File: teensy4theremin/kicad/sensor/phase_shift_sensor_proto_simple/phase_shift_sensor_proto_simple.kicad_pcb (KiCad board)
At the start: 2 copper layers, 94 x 35.6 mm, 23 parts, among them J1 INDUCTOR_IN, J2 INDUCTOR_OUT, J3 ANTENNA, J4 SENSOR, U1 74HC04, U2 sp721, U3 REG_3V3

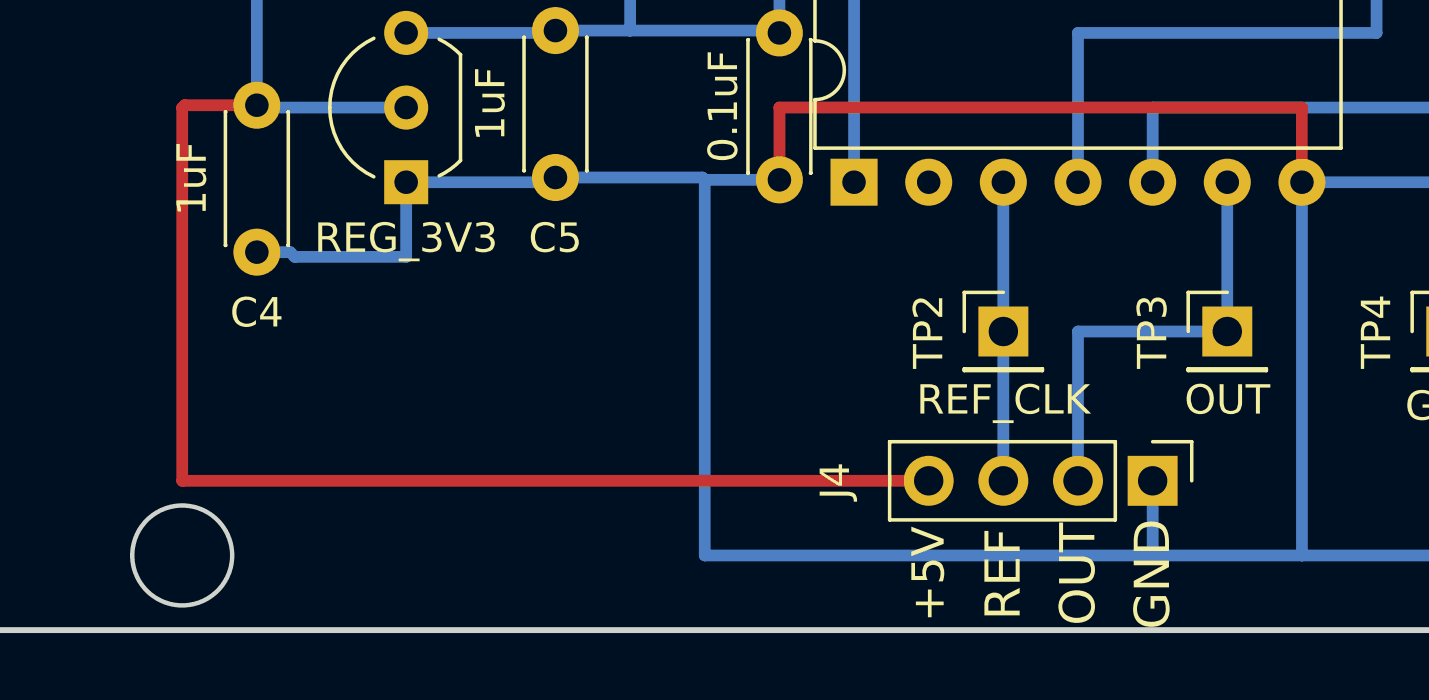
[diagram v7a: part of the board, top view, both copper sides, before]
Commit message: update phase shift sensor prototype PCB - change connector to 5-pin one, with additional ground
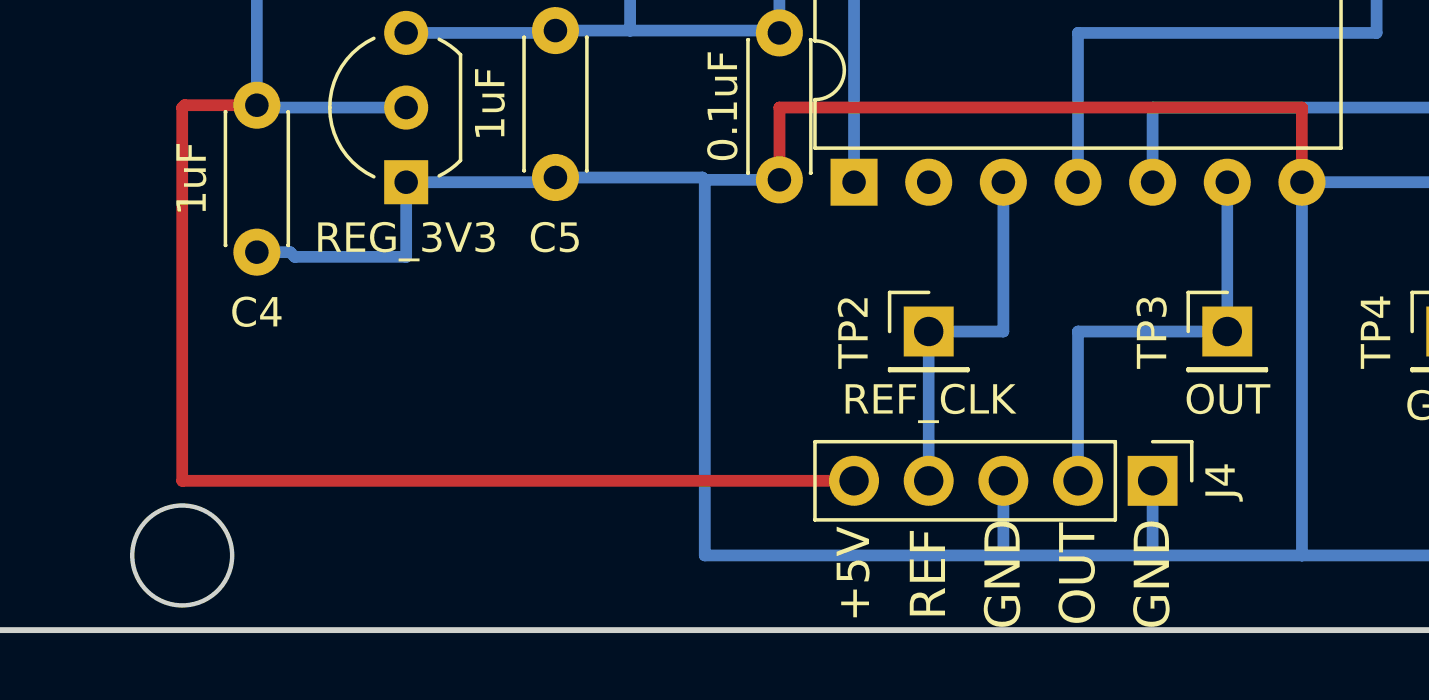
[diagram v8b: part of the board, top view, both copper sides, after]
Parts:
- J4: footprint Connector_PinHeader_2.54mm:PinHeader_1x04_P2.54mm_Vertical -> Connector_PinHeader_2.54mm:PinHeader_1x05_P2.54mm_Vertical
- moved TP2 2.54 mm to (94.0, 111.8)
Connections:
- J4 pad 3: /REF_CLK -> GND
- J4 pad 4: +5V -> /REF_CLK
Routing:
- net +5V: track 50.8 -> 48.2 mm
- net /REF_CLK: track 10.2 -> 12.7 mm
- net GND: track 142.7 -> 145.2 mm
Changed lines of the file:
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@@
   (general
     (thickness 1.6)
-    (drawings 16)
-    (tracks 90)
+    (drawings 17)
+    (tracks 94)
     (zones 0)
     (modules 23)
@@
     (add_net "Net-(U2-Pad6)")
   )
+  (module Connector_PinHeader_2.54mm:PinHeader_1x05_P2.54mm_Vertical (layer F.Cu)
+    (at 101.6 116.84 270)
+    (descr "Through hole straight pin header, 1x05, 2.54mm pitch, single row")
+    (tags "Through hole pin header THT 1x05 2.54mm single row")
+    (fp_text reference J4 (at 0 -2.33 270) (layer F.SilkS)
+      (effects (font (size 1 1) (thickness 0.15)))
+    )
+    (fp_text value SENSOR (at 0 12.49 270) (layer F.Fab)
+      (effects (font (size 1 1) (thickness 0.15)))
+    )
+    (fp_line (start -0.635 -1.27) (end 1.27 -1.27) (layer F.Fab) (width 0.1))
+    (fp_line (start 1.27 -1.27) (end 1.27 11.43) (layer F.Fab) (width 0.1))
+    (fp_line (start 1.27 11.43) (end -1.27 11.43) (layer F.Fab) (width 0.1))
+    (fp_line (start -1.27 11.43) (end -1.27 -0.635) (layer F.Fab) (width 0.1))
+    (fp_line (start -1.27 -0.635) (end -0.635 -1.27) (layer F.Fab) (width 0.1))
+    (fp_line (start -1.33 11.49) (end 1.33 11.49) (layer F.SilkS) (width 0.12))
+    (fp_line (start -1.33 1.27) (end -1.33 11.49) (layer F.SilkS) (width 0.12))
+    (fp_line (start 1.33 1.27) (end 1.33 11.49) (layer F.SilkS) (width 0.12))
+    (fp_line (start -1.33 1.27) (end 1.33 1.27) (layer F.SilkS) (width 0.12))
+    (fp_line (start -1.33 0) (end -1.33 -1.33) (layer F.SilkS) (width 0.12))
+    (fp_line (start -1.33 -1.33) (end 0 -1.33) (layer F.SilkS) (width 0.12))
+    (fp_line (start -1.8 -1.8) (end -1.8 11.95) (layer F.CrtYd) (width 0.05))
+    (fp_line (start -1.8 11.95) (end 1.8 11.95) (layer F.CrtYd) (width 0.05))
+    (fp_line (start 1.8 11.95) (end 1.8 -1.8) (layer F.CrtYd) (width 0.05))
+    (fp_line (start 1.8 -1.8) (end -1.8 -1.8) (layer F.CrtYd) (width 0.05))
+    (fp_text user %R (at 0 5.08) (layer F.Fab)
+      (effects (font (size 1 1) (thickness 0.15)))
+    )
+    (pad 1 thru_hole rect (at 0 0 270) (size 1.7 1.7) (drill 1) (layers *.Cu *.Mask)
+      (net 2 GND))
+    (pad 2 thru_hole oval (at 0 2.54 270) (size 1.7 1.7) (drill 1) (layers *.Cu *.Mask)
+      (net 17 /OUT))
+    (pad 3 thru_hole oval (at 0 5.08 270) (size 1.7 1.7) (drill 1) (layers *.Cu *.Mask)
+      (net 2 GND))
+    (pad 4 thru_hole oval (at 0 7.62 270) (size 1.7 1.7) (drill 1) (layers *.Cu *.Mask)
+      (net 5 /REF_CLK))
+    (pad 5 thru_hole oval (at 0 10.16 270) (size 1.7 1.7) (drill 1) (layers *.Cu *.Mask)
+      (net 7 +5V))
+    (model ${KISYS3DMOD}/Connector_PinHeader_2.54mm.3dshapes/PinHeader_1x05_P2.54mm_Vertical.wrl
+      (at (xyz 0 0 0))
+      (scale (xyz 1 1 1))
+      (rotate (xyz 0 0 0))
+    )
+  )
   (module Connector_PinHeader_2.54mm:PinHeader_1x01_P2.54mm_Vertical (layer F.Cu)
     (at 71.12 99.06)
@@
   )
   (module Connector_PinHeader_2.54mm:PinHeader_1x01_P2.54mm_Vertical (layer F.Cu)
-    (at 96.52 111.76)
+    (at 93.98 111.76)
     (descr "Through hole straight pin header, 1x01, 2.54mm pitch, single row")
     (tags "Through hole pin header THT 1x01 2.54mm single row")
@@
       (net 15 "Net-(J1-Pad1)"))
     (model ${KISYS3DMOD}/Connector_PinHeader_2.54mm.3dshapes/PinHeader_1x02_P2.54mm_Vertical.wrl
-      (at (xyz 0 0 0))
-      (scale (xyz 1 1 1))
-      (rotate (xyz 0 0 0))
-    )
-  )
-  (module Connector_PinHeader_2.54mm:PinHeader_1x04_P2.54mm_Vertical (layer F.Cu)
-    (at 101.6 116.84 270)
-    (descr "Through hole straight pin header, 1x04, 2.54mm pitch, single row")
-    (tags "Through hole pin header THT 1x04 2.54mm single row")
-    (fp_text reference J4 (at 0 10.795 270) (layer F.SilkS)
-      (effects (font (size 1 1) (thickness 0.15)))
-    )
-    (fp_text value SENSOR (at 1.905 -3.175 90) (layer F.Fab)
-      (effects (font (size 1 1) (thickness 0.15)))
-    )
-    (fp_line (start -0.635 -1.27) (end 1.27 -1.27) (layer F.Fab) (width 0.1))
-    (fp_line (start 1.27 -1.27) (end 1.27 8.89) (layer F.Fab) (width 0.1))
-    (fp_line (start 1.27 8.89) (end -1.27 8.89) (layer F.Fab) (width 0.1))
-    (fp_line (start -1.27 8.89) (end -1.27 -0.635) (layer F.Fab) (width 0.1))
-    (fp_line (start -1.27 -0.635) (end -0.635 -1.27) (layer F.Fab) (width 0.1))
-    (fp_line (start -1.33 8.95) (end 1.33 8.95) (layer F.SilkS) (width 0.12))
-    (fp_line (start -1.33 1.27) (end -1.33 8.95) (layer F.SilkS) (width 0.12))
-    (fp_line (start 1.33 1.27) (end 1.33 8.95) (layer F.SilkS) (width 0.12))
-    (fp_line (start -1.33 1.27) (end 1.33 1.27) (layer F.SilkS) (width 0.12))
-    (fp_line (start -1.33 0) (end -1.33 -1.33) (layer F.SilkS) (width 0.12))
-    (fp_line (start -1.33 -1.33) (end 0 -1.33) (layer F.SilkS) (width 0.12))
-    (fp_line (start -1.8 -1.8) (end -1.8 9.4) (layer F.CrtYd) (width 0.05))
-    (fp_line (start -1.8 9.4) (end 1.8 9.4) (layer F.CrtYd) (width 0.05))
-    (fp_line (start 1.8 9.4) (end 1.8 -1.8) (layer F.CrtYd) (width 0.05))
-    (fp_line (start 1.8 -1.8) (end -1.8 -1.8) (layer F.CrtYd) (width 0.05))
-    (fp_text user %R (at 0 3.81) (layer F.Fab)
-      (effects (font (size 1 1) (thickness 0.15)))
-    )
-    (pad 1 thru_hole rect (at 0 0 270) (size 1.7 1.7) (drill 1) (layers *.Cu *.Mask)
-      (net 2 GND))
-    (pad 2 thru_hole oval (at 0 2.54 270) (size 1.7 1.7) (drill 1) (layers *.Cu *.Mask)
-      (net 17 /OUT))
-    (pad 3 thru_hole oval (at 0 5.08 270) (size 1.7 1.7) (drill 1) (layers *.Cu *.Mask)
-      (net 5 /REF_CLK))
-    (pad 4 thru_hole oval (at 0 7.62 270) (size 1.7 1.7) (drill 1) (layers *.Cu *.Mask)
-      (net 7 +5V))
-    (model ${KISYS3DMOD}/Connector_PinHeader_2.54mm.3dshapes/PinHeader_1x04_P2.54mm_Vertical.wrl
       (at (xyz 0 0 0))
       (scale (xyz 1 1 1))
@@
     )
   )
+  (gr_text GND (at 96.52 120.015 90) (layer F.SilkS)
+    (effects (font (size 1.2 1.2) (thickness 0.3)))
+  )
   (gr_text * (at 93.345 89.535) (layer F.SilkS)
     (effects (font (size 1.5 1.5) (thickness 0.3)) (justify mirror))
@@
     (effects (font (size 1.2 1.2) (thickness 0.3)))
   )
-  (gr_text REF (at 96.52 120.015 90) (layer F.SilkS)
+  (gr_text REF (at 93.98 120.015 90) (layer F.SilkS)
     (effects (font (size 1.2 1.2) (thickness 0.3)))
   )
-  (gr_text +5V (at 93.98 120.015 90) (layer F.SilkS)
+  (gr_text +5V (at 91.44 120.015 90) (layer F.SilkS)
     (effects (font (size 1.1 1.1) (thickness 0.275)))
   )
@@
   (segment (start 76.2 109.22) (end 76.2 106.68) (width 0.4) (layer B.Cu) (net 2))
   (segment (start 124.46 106.68) (end 124.46 109.22) (width 0.4) (layer B.Cu) (net 2))
-  (segment (start 101.6 119.38) (end 86.36 119.38) (width 0.4) (layer B.Cu) (net 2))
   (segment (start 124.46 109.22) (end 119.38 109.22) (width 0.4) (layer B.Cu) (net 2))
   (segment (start 119.38 109.22) (end 111.76 109.22) (width 0.4) (layer B.Cu) (net 2))
@@
   (segment (start 88.9 104.14) (end 88.9 106.6) (width 0.4) (layer F.Cu) (net 2))
   (segment (start 106.68 104.14) (end 88.9 104.14) (width 0.4) (layer F.Cu) (net 2))
-  (segment (start 96.52 116.84) (end 96.52 106.68) (width 0.4) (layer B.Cu) (net 5))
+  (segment (start 96.52 116.84) (end 96.52 119.38) (width 0.4) (layer B.Cu) (net 2))
+  (segment (start 101.6 119.38) (end 96.52 119.38) (width 0.4) (layer B.Cu) (net 2))
+  (segment (start 96.52 119.38) (end 86.36 119.38) (width 0.4) (layer B.Cu) (net 2))
+  (segment (start 93.98 116.84) (end 93.98 111.76) (width 0.4) (layer B.Cu) (net 5))
+  (segment (start 93.98 111.76) (end 96.52 111.76) (width 0.4) (layer B.Cu) (net 5))
+  (segment (start 96.52 111.76) (end 96.52 106.68) (width 0.4) (layer B.Cu) (net 5))
   (segment (start 71.2 104.14) (end 71.12 104.06) (width 0.4) (layer B.Cu) (net 7))
   (segment (start 76.2 104.14) (end 71.2 104.14) (width 0.4) (layer B.Cu) (net 7))
   (segment (start 71.12 104.06) (end 71.12 99.06) (width 0.4) (layer B.Cu) (net 7))
-  (segment (start 68.58 116.84) (end 93.98 116.84) (width 0.4) (layer F.Cu) (net 7))
+  (segment (start 68.58 116.84) (end 91.44 116.84) (width 0.4) (layer F.Cu) (net 7))
   (segment (start 68.58 104.14) (end 68.58 116.84) (width 0.4) (layer F.Cu) (net 7))
   (segment (start 71.12 104.06) (end 68.66 104.06) (width 0.4) (layer F.Cu) (net 7))
@@
   (segment (start 142.24 104.14) (end 142.24 109.22) (width 0.4) (layer B.Cu) (net 16))
   (segment (start 142.24 106.68) (end 142.32 106.68) (width 0.4) (layer B.Cu) (net 16))
+  (segment (start 104.14 111.76) (end 104.14 106.68) (width 0.4) (layer B.Cu) (net 17))
+  (segment (start 99.06 116.84) (end 99.06 111.76) (width 0.4) (layer B.Cu) (net 17))
+  (segment (start 99.06 111.76) (end 104.14 111.76) (width 0.4) (layer B.Cu) (net 17))
   (segment (start 129.54 106.68) (end 129.54 104.14) (width 0.4) (layer B.Cu) (net 18))
   (segment (start 101.6 104.14) (end 101.6 106.68) (width 0.4) (layer B.Cu) (net 18))
@@
   (segment (start 121.92 104.14) (end 101.6 104.14) (width 0.4) (layer B.Cu) (net 18))
   (segment (start 129.54 106.68) (end 129.54 109.22) (width 0.4) (layer B.Cu) (net 18))
-  (segment (start 142.16 99.06) (end 142.24 99.14) (width 0.4) (layer B.Cu) (net 19))
-  (segment (start 104.14 111.76) (end 104.14 106.68) (width 0.4) (layer B.Cu) (net 17))
-  (segment (start 99.06 116.84) (end 99.06 111.76) (width 0.4) (layer B.Cu) (net 17))
-  (segment (start 99.06 111.76) (end 104.14 111.76) (width 0.4) (layer B.Cu) (net 17))
   (segment (start 129.62 104.06) (end 129.54 104.14) (width 0.4) (layer B.Cu) (net 18))
   (segment (start 137.16 104.06) (end 129.62 104.06) (width 0.4) (layer B.Cu) (net 18))
   (segment (start 129.54 109.22) (end 134.62 109.22) (width 0.4) (layer B.Cu) (net 18))
+  (segment (start 142.16 99.06) (end 142.24 99.14) (width 0.4) (layer B.Cu) (net 19))
   (segment (start 137.24 99.14) (end 137.16 99.06) (width 0.4) (layer B.Cu) (net 19))
   (segment (start 142.24 99.14) (end 137.24 99.14) (width 0.4) (layer B.Cu) (net 19))
